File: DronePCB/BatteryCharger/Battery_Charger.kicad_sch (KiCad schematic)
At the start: 43 parts, among them Q1 AO3400A, Q2 AO3400A, Q3 SiS454DN, Q4 SiS454DN, Q5 AO3400A, U1 BQ24725A

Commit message: Add files via upload
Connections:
- net at C2.1, C3.1, C8.1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: no longer D2.3, R9.1
- new net: D2.3, R9.1
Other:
- moved on the sheet: D2
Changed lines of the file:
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@@
 	)
 	(junction
-		(at 128.27 26.67)
-		(diameter 0)
-		(color 0 0 0 0)
-	)
-	(junction
 		(at 124.46 68.58)
 		(diameter 0)
@@
 	(wire
 		(pts
-			(xy 135.89 21.59) (xy 186.69 21.59)
+			(xy 135.89 20.32) (xy 186.69 20.32)
 		)
 		(stroke
@@
 	(wire
 		(pts
-			(xy 186.69 21.59) (xy 186.69 26.67)
+			(xy 186.69 20.32) (xy 186.69 26.67)
 		)
 		(stroke
@@
 	(wire
 		(pts
-			(xy 128.27 26.67) (xy 73.66 26.67)
-		)
-		(stroke
-			(width 0)
-			(type default)
-		)
-	)
-	(wire
-		(pts
 			(xy 144.78 82.55) (xy 135.89 82.55)
 		)
@@
 	(wire
 		(pts
-			(xy 120.65 21.59) (xy 120.65 16.51)
+			(xy 120.65 20.32) (xy 120.65 16.51)
 		)
 		(stroke
@@
 	(wire
 		(pts
-			(xy 128.27 26.67) (xy 128.27 29.21)
+			(xy 157.48 49.53) (xy 157.48 26.67)
 		)
 		(stroke
@@
 	(wire
 		(pts
-			(xy 157.48 49.53) (xy 157.48 26.67)
+			(xy 71.12 86.36) (xy 49.53 86.36)
 		)
 		(stroke
@@
 	(wire
 		(pts
-			(xy 71.12 86.36) (xy 49.53 86.36)
+			(xy 25.4 63.5) (xy 25.4 64.77)
 		)
 		(stroke
@@
 	(wire
 		(pts
-			(xy 25.4 63.5) (xy 25.4 64.77)
+			(xy 83.82 58.42) (xy 41.91 58.42)
 		)
 		(stroke
@@
 	(wire
 		(pts
-			(xy 83.82 58.42) (xy 41.91 58.42)
+			(xy 186.69 58.42) (xy 186.69 90.17)
 		)
 		(stroke
@@
 	(wire
 		(pts
-			(xy 186.69 58.42) (xy 186.69 90.17)
+			(xy 78.74 96.52) (xy 78.74 97.79)
 		)
 		(stroke
@@
 	(wire
 		(pts
-			(xy 78.74 96.52) (xy 78.74 97.79)
+			(xy 128.27 25.4) (xy 128.27 29.21)
 		)
 		(stroke
@@
 	(wire
 		(pts
+			(xy 73.66 26.67) (xy 157.48 26.67)
+		)
+		(stroke
+			(width 0)
+			(type default)
+		)
+	)
+	(wire
+		(pts
 			(xy 186.69 53.34) (xy 186.69 58.42)
 		)
@@
 		)
 	)
-	(wire
-		(pts
-			(xy 157.48 26.67) (xy 128.27 26.67)
-		)
-		(stroke
-			(width 0)
-			(type default)
-		)
-	)
 	(symbol
 		(lib_id "Device:R")
@@
 	(symbol
 		(lib_id "Diode:BAT54C")
-		(at 128.27 21.59 0)
+		(at 128.27 20.32 0)
 		(unit 1)
 		(body_style 1)
@@
 		(fields_autoplaced yes)
 		(property "Reference" "D2"
-			(at 128.27 15.24 0)
+			(at 128.27 13.97 0)
 			(show_name no)
 			(do_not_autoplace no)
@@
 		)
 		(property "Value" "BAT54C"
-			(at 128.27 17.78 0)
+			(at 128.27 16.51 0)
 			(show_name no)
 			(do_not_autoplace no)
@@
 		)
 		(property "Footprint" "Package_TO_SOT_SMD:SOT-23"
-			(at 130.175 18.415 0)
+			(at 130.175 17.145 0)
 			(hide yes)
 			(show_name no)
@@
 		)
 		(property "Datasheet" "http://www.diodes.com/_files/datasheets/ds11005.pdf"
-			(at 126.238 21.59 0)
+			(at 126.238 20.32 0)
 			(hide yes)
 			(show_name no)
@@
 		)
 		(property "Description" "dual schottky barrier diode, common cathode"
-			(at 128.27 21.59 0)
+			(at 128.27 20.32 0)
 			(hide yes)
 			(show_name no)

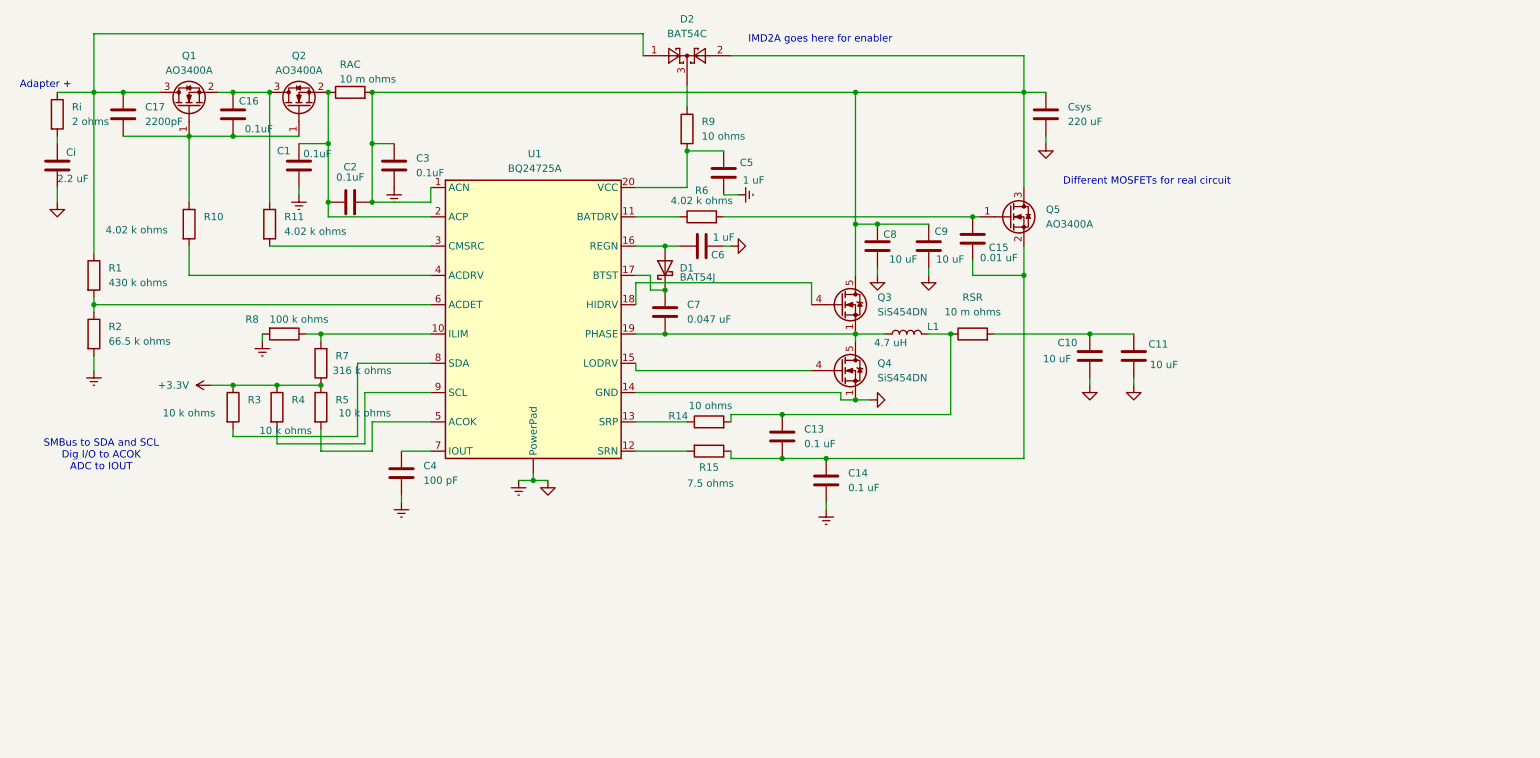
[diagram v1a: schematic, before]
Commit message: Added IR circuit to main schematic | fixed RPi header gnd
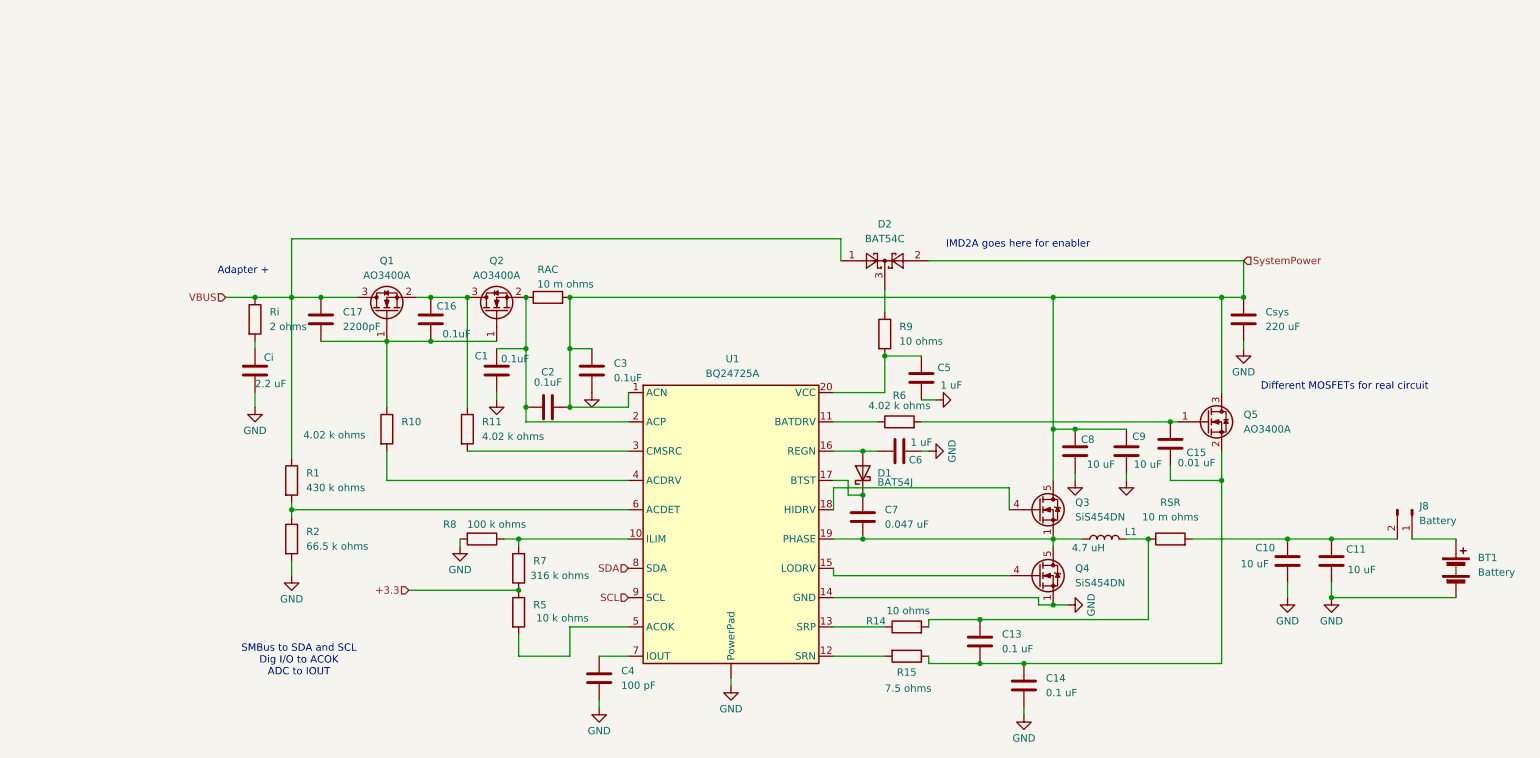
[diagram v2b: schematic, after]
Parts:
- removed R3, R4: 10 k ohms, symbol Device:R
- added BT1: Battery, symbol Device:Battery
- added J8: Battery, Connector_PinHeader_2.54mm:PinHeader_1x02_P2.54mm_Vertical, symbol Connector:Conn_01x02_Pin
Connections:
- net VBUS: now reaches C17.1, D2.1, Q1.3 (D), R1.1, Ri.1
- net SystemPower: now reaches C2.1, C3.1, C8.1, C9.1, Csys.1, D2.2, Q3.5 (D), Q5.3 (D), RAC.2, U1.1 (ACN)
- net SDA: now reaches U1.8 (SDA)
- net SCL: now reaches U1.9 (SCL)
- net at C10.1, C11.1, RSR.2: now also J8.2 (Pin_2)
- net +3.3V renamed +3.3
- net GND1 renamed GND
- net GND: now also BT1.2 (-)
- new net: BT1.1 (+), J8.1 (Pin_1)
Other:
- moved on the sheet: C1, C10, C11, C13, C14, C15, C16, C17, C2, C3, C4, C5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

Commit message: Completed H-Bridge Circuit | Finished Schematic | Working on pcb design
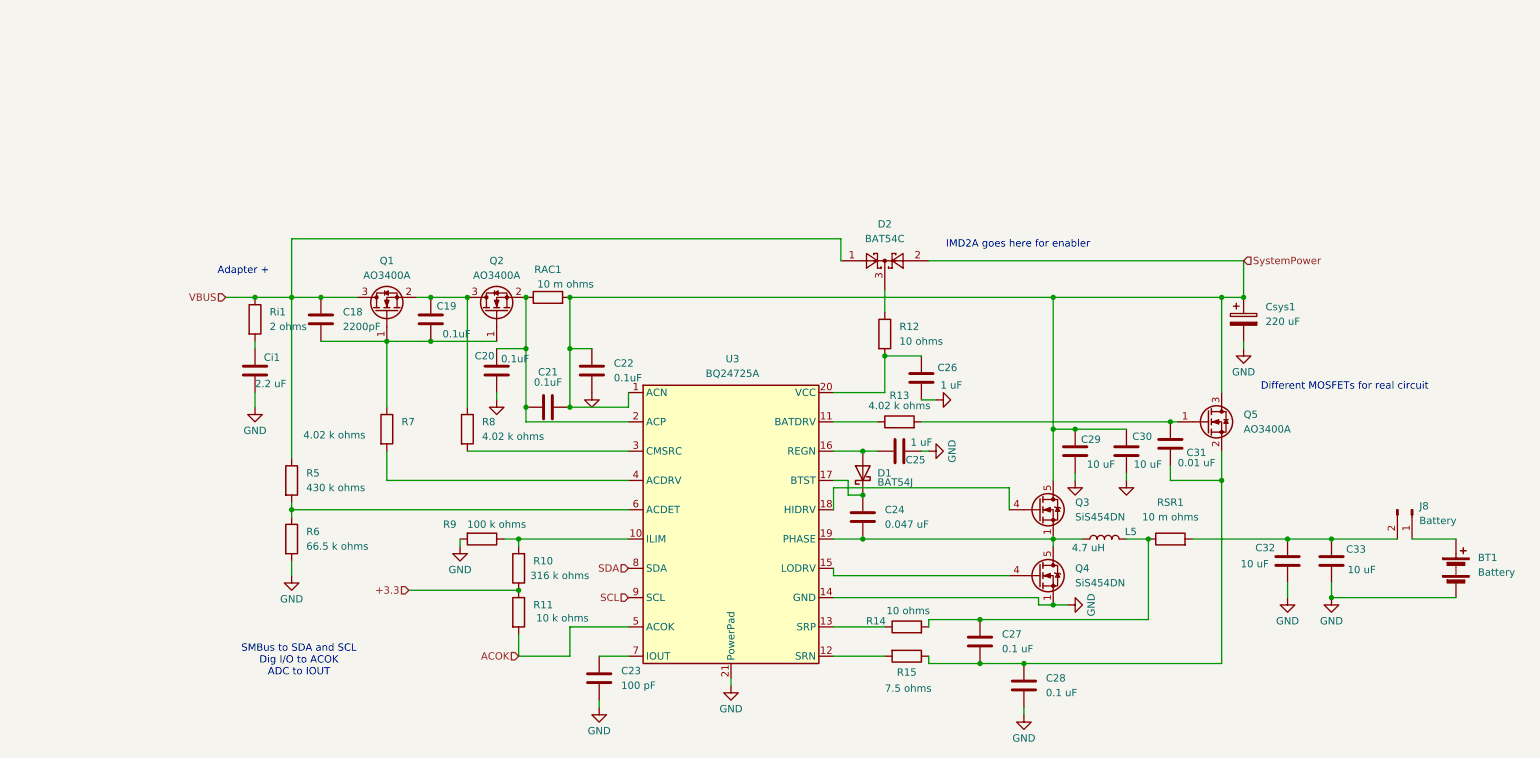
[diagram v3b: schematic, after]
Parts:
- BT1: footprint (none) -> Connector_Wire:SolderWire-0.5sqmm_1x02_P4.6mm_D0.9mm_OD2.1mm_Relief
- C18: renamed from C17; footprint (none) -> Capacitor_SMD:C_0603_1608Metric
- C19: renamed from C16; footprint (none) -> Capacitor_SMD:C_0603_1608Metric
- C20: renamed from C1; footprint (none) -> Capacitor_SMD:C_0603_1608Metric
- C21: renamed from C2; footprint (none) -> Capacitor_SMD:C_0603_1608Metric
- C22: renamed from C3; footprint (none) -> Capacitor_SMD:C_0603_1608Metric
- C23: renamed from C4; footprint (none) -> Capacitor_SMD:C_0603_1608Metric
- C24: renamed from C7; footprint (none) -> Capacitor_SMD:C_0603_1608Metric
- C25: renamed from C6; footprint (none) -> Capacitor_SMD:C_0603_1608Metric
- C26: renamed from C5; footprint (none) -> Capacitor_SMD:C_0603_1608Metric
- C27: renamed from C13; footprint (none) -> Capacitor_SMD:C_0603_1608Metric
- C28: renamed from C14; footprint (none) -> Capacitor_SMD:C_0603_1608Metric
- C29: renamed from C8; footprint (none) -> Capacitor_SMD:C_0603_1608Metric
- C30: renamed from C9; footprint (none) -> Capacitor_SMD:C_0603_1608Metric
- C31: renamed from C15; footprint (none) -> Capacitor_SMD:C_0603_1608Metric
- C32: renamed from C10; footprint (none) -> Capacitor_SMD:C_0603_1608Metric
- C33: renamed from C11; footprint (none) -> Capacitor_SMD:C_0603_1608Metric
- Ci1: renamed from Ci; footprint (none) -> Capacitor_SMD:C_0603_1608Metric
- Csys1: renamed from Csys; footprint (none) -> Capacitor_THT:CP_Radial_D6.3mm_P2.50mm; symbol Device:C -> Device:C_Polarized
- L5: renamed from L1; footprint (none) -> Inductor_SMD:L_Vishay_IHLP-2525
- R10: renamed from R7; footprint (none) -> Resistor_SMD:R_0603_1608Metric
- R11: renamed from R5; footprint (none) -> Resistor_SMD:R_0603_1608Metric
- R12: renamed from R9; footprint (none) -> Resistor_SMD:R_0603_1608Metric
- R13: renamed from R6; footprint (none) -> Resistor_SMD:R_0603_1608Metric
- R14, R15: footprint (none) -> Resistor_SMD:R_0603_1608Metric
- R5: renamed from R1; footprint (none) -> Resistor_SMD:R_0603_1608Metric
- R6: renamed from R2; footprint (none) -> Resistor_SMD:R_0603_1608Metric
- R7: renamed from R10; footprint (none) -> Resistor_SMD:R_0603_1608Metric
- R8: renamed from R11; footprint (none) -> Resistor_SMD:R_0603_1608Metric
- R9: renamed from R8; footprint (none) -> Resistor_SMD:R_0603_1608Metric
- RAC1: renamed from RAC; footprint (none) -> Resistor_SMD:R_0603_1608Metric
- RSR1: renamed from RSR; footprint (none) -> Resistor_SMD:R_0603_1608Metric
- Ri1: renamed from Ri; footprint (none) -> Resistor_SMD:R_0603_1608Metric
- U3: renamed from U1; footprint (none) -> ExternalParts:QFN50P350X350X100-21N
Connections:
- net GND: now also U3.21 (PowerPad); no longer U3. (PowerPad)
- net ACOK: now reaches R11.2, U3.5 (ACOK)

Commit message: Add files via upload
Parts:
- removed BT1: Battery, Connector_Wire:SolderWire-0.5sqmm_1x02_P4.6mm_D0.9mm_OD2.1mm_Relief, symbol Device:Battery
- removed J8: Battery, Connector_PinHeader_2.54mm:PinHeader_1x02_P2.54mm_Vertical, symbol Connector:Conn_01x02_Pin
- removed Q3, Q4: SiS454DN, Package_SO:Vishay_PowerPAK_1212-8_Single, symbol Transistor_FET:SiS454DN
- added MOSFET1, MOSFET2: SIS412DN-T1-GE3, POWERPAK_1212-8, symbol SIS412DN-T1-GE3:SIS412DN-T1-GE3
- added R3, R4: 10 k ohms, symbol Device:R
- C1: renamed from C20; footprint Capacitor_SMD:C_0603_1608Metric -> (none)
- C10: renamed from C32; footprint Capacitor_SMD:C_0603_1608Metric -> (none)
- C11: renamed from C33; footprint Capacitor_SMD:C_0603_1608Metric -> (none)
- C13: renamed from C27; footprint Capacitor_SMD:C_0603_1608Metric -> (none)
- C14: renamed from C28; footprint Capacitor_SMD:C_0603_1608Metric -> (none)
- C15: renamed from C31; footprint Capacitor_SMD:C_0603_1608Metric -> (none)
- C16: renamed from C19; footprint Capacitor_SMD:C_0603_1608Metric -> (none)
- C17: renamed from C18; footprint Capacitor_SMD:C_0603_1608Metric -> (none)
- C2: renamed from C21; footprint Capacitor_SMD:C_0603_1608Metric -> (none)
- C3: renamed from C22; footprint Capacitor_SMD:C_0603_1608Metric -> (none)
- C4: renamed from C23; footprint Capacitor_SMD:C_0603_1608Metric -> (none)
- C5: renamed from C26; footprint Capacitor_SMD:C_0603_1608Metric -> (none)
- C6: renamed from C25; footprint Capacitor_SMD:C_0603_1608Metric -> (none)
- C7: renamed from C24; footprint Capacitor_SMD:C_0603_1608Metric -> (none)
- C8: renamed from C29; footprint Capacitor_SMD:C_0603_1608Metric -> (none)
- C9: renamed from C30; footprint Capacitor_SMD:C_0603_1608Metric -> (none)
- Ci: renamed from Ci1; footprint Capacitor_SMD:C_0603_1608Metric -> (none)
- Csys: renamed from Csys1; footprint Capacitor_THT:CP_Radial_D6.3mm_P2.50mm -> (none); symbol Device:C_Polarized -> Device:C
- L1: renamed from L5; footprint Inductor_SMD:L_Vishay_IHLP-2525 -> (none)
- Q1: footprint Package_TO_SOT_SMD:SOT-23 -> FDS6680A:SOIC127P600X175-8N; symbol Transistor_FET:AO3400A -> FDS6680A:FDS6680A; A1_MIN (none) -> 0.1; A_MIN (none) -> 1.75; A_NOM (none) -> 1.75; B_MAX (none) -> 0.51; B_MIN (none) -> 0.33; B_NOM (none) -> 0.42; Check_prices (none) -> https://www.snapeda.com/parts/FDS6680A/Onsemi/view-part/?re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; D2_MAX (none) -> 0.0; D_MAX (none) -> 5.0; D_MIN (none) -> 4.8; D_NOM (none) -> 4.9; DigiKey_Part_Number (none) -> FDS6680ACT-ND; E1_MAX (none) -> 4.0; E1_MIN (none) -> 3.8; E1_NOM (none) -> 3.9; E2_MAX (none) -> 0.0; ENOM (none) -> 1.27; E_MAX (none) -> 6.2; E_MIN (none) -> 5.8; E_NOM (none) -> 6.0; L_MAX (none) -> 0.9; L_MIN (none) -> 0.4; L_NOM (none) -> 0.65; MANUFACTURER (none) -> ON Semiconductor; MAXIMUM_PACKAGE_HEIGHT (none) -> 1.75mm; MF (none) -> ON Semiconductor; MP (none) -> FDS6680A; PARTREV (none) -> 6; PIN_COUNT (none) -> 8.0; Package (none) -> SO-8 ON Semiconductor; STANDARD (none) -> IPC 7351B; SnapEDA_Link (none) -> https://www.snapeda.com/parts/FDS6680A/Onsemi/view-part/?re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
- Q2, Q5: footprint Package_TO_SOT_SMD:SOT-23 -> FDS6680A:SOIC127P600X175-8N; symbol Transistor_FET:AO3400A -> FDS6680A:FDS6680A
- R1: renamed from R5; footprint Resistor_SMD:R_0603_1608Metric -> (none)
- R10: renamed from R7; footprint Resistor_SMD:R_0603_1608Metric -> (none)
- R11: renamed from R8; footprint Resistor_SMD:R_0603_1608Metric -> (none)
- R14, R15: footprint Resistor_SMD:R_0603_1608Metric -> (none)
- R2: renamed from R6; footprint Resistor_SMD:R_0603_1608Metric -> (none)
- R5: renamed from R11; footprint Resistor_SMD:R_0603_1608Metric -> (none)
- R6: renamed from R13; footprint Resistor_SMD:R_0603_1608Metric -> (none)
- R7: renamed from R10; footprint Resistor_SMD:R_0603_1608Metric -> (none)
- R8: renamed from R9; footprint Resistor_SMD:R_0603_1608Metric -> (none)
- R9: renamed from R12; footprint Resistor_SMD:R_0603_1608Metric -> (none)
- RAC: renamed from RAC1; footprint Resistor_SMD:R_0603_1608Metric -> (none)
- RSR: renamed from RSR1; footprint Resistor_SMD:R_0603_1608Metric -> (none)
- Ri: renamed from Ri1; footprint Resistor_SMD:R_0603_1608Metric -> (none)
- U1: renamed from U3; footprint ExternalParts:QFN50P350X350X100-21N -> (none)
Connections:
- net at C1.1, C2.2, RAC.1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: now also Q2.5, Q2.6, Q2.7, Q2.8; no longer Q2.2 (S)
- net at C7.2, L1.1, U1.19 (PHASE): now also MOSFET1.1 (S), MOSFET2.8 (D)
- net at U1.15 (LODRV): now also MOSFET2.4 (G)
- net at U1.18 (HIDRV): now also MOSFET1.4 (G)
- net at C16.2, C17.2, R10.1: now also Q1.4, Q2.4; no longer Q1.1 (G), Q2.1 (G)
- net at C16.1, Q1.2, Q2.3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: now also Q1.1, Q1.3, Q2.1, Q2.2
- net at C13.2, C14.1, C15.2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: now also Q5.1, Q5.3
- net at C15.1, R6.2: now also Q5.4; no longer Q5.1 (G)
- net +3.3 renamed +3.3V
- net +3.3V: now also R3.1, R4.1
- net ACOK: no longer names the net of R5.2, U1.5 (ACOK)
- net GND renamed GND1
- net GND1: now also U1. (PowerPad), MOSFET2.1 (S); no longer U1.21 (PowerPad)
- net SCL: no longer names the net of U1.9 (SCL)
- net SCL: now also R4.2
- net SDA: no longer names the net of U1.8 (SDA)
- net SDA: now also R3.2
- net SystemPower: no longer names the net of C2.1, C3.1, C8.1, C9.1, Csys.1, D2.2, RAC.2, U1.1 (ACN)
- net SystemPower: now also Q5.5, Q5.6, Q5.7, Q5.8, MOSFET1.8 (D); no longer Q5.3 (D)
- net VBUS: no longer names the net of C17.1, D2.1, R1.1, Ri.1
- net VBUS: now also Q1.5, Q1.6, Q1.7, Q1.8; no longer Q1.3 (D)
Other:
- moved on the sheet: C1, C10, C11, C13, C14, C15, C16, C17, C2, C3, C4, C5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
